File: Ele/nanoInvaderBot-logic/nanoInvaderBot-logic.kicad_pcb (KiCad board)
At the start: 2 copper layers, 72 x 40 mm, 16 parts, among them J1 S6B-ZR-SM4A-TF(LF)(SN), J2 S6B-ZR-SM4A-TF(LF)(SN), J3 1746142-1, J4 Conn_01x20, P1 USB_C_Plug_USB2.0, U4 BQ25170DSGR, U5 TLV61048DBVT

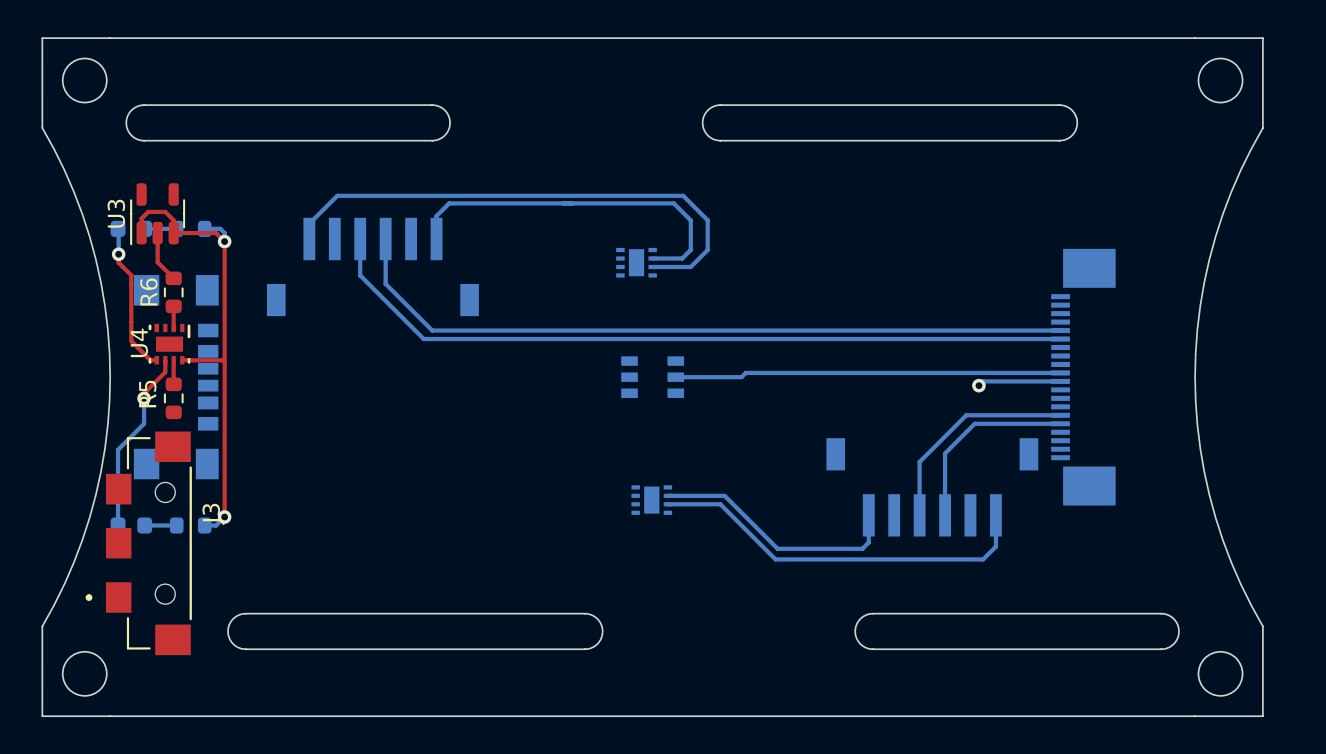
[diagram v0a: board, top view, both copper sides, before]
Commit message: Power side done, logic side cleanup
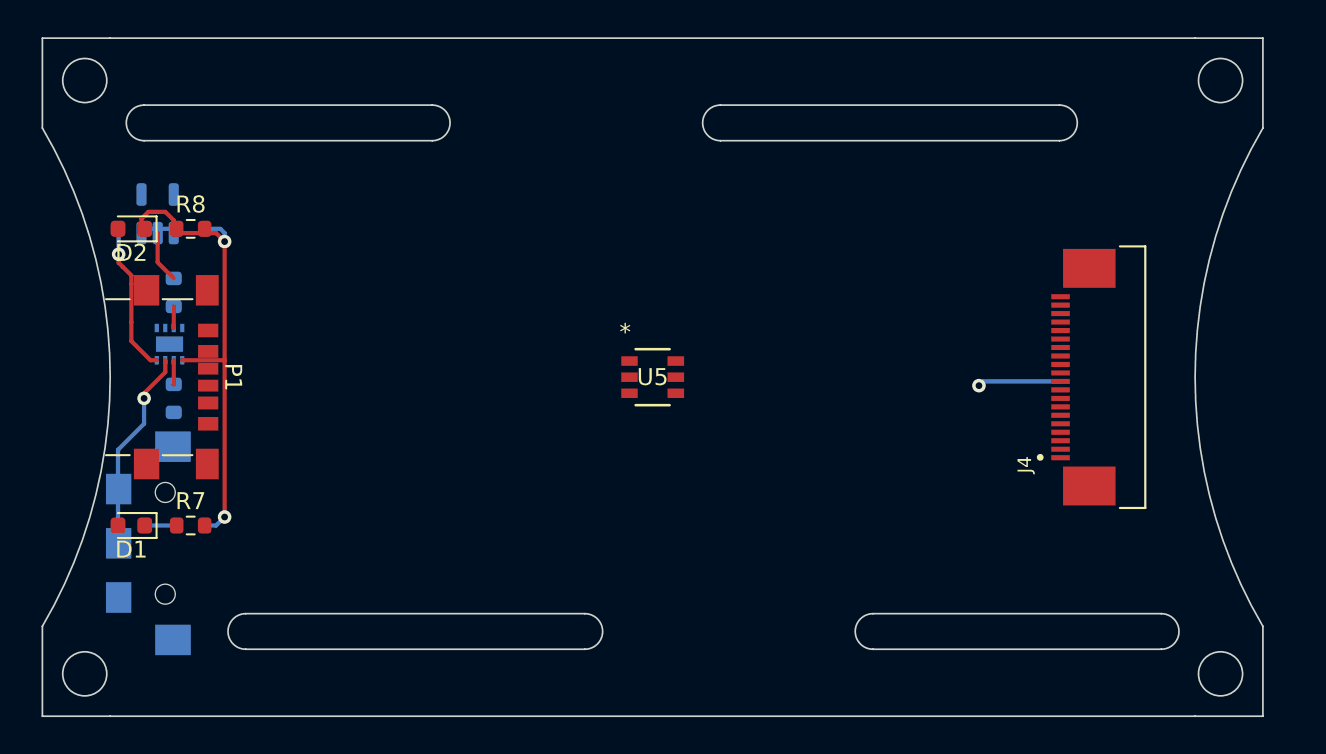
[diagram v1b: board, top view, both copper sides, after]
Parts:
- removed J1, J2: S6B-ZR-SM4A-TF(LF)(SN), footprints:JST_S6B-ZR-SM4A-TF(LF)(SN)
- removed U1, U2: ~, Package_SON:WSON-8-1EP_2x2mm_P0.5mm_EP0.9x1.6mm
- D1, D2, J4, P1, R7, R8, U5: moved to F.Cu
- J3, R5, R6, U3, U4: moved to B.Cu
- turned D1 to 180 degrees
- turned D2 to 180 degrees
- turned J3 to 90 degrees
- turned J4 to 90 degrees
- turned P1 to -90 degrees
- turned R7 to 0 degrees
- turned R8 to 0 degrees
- turned U5 to 0 degrees
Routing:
- net /MOTOR1_ENC2: track 45.0 -> 0.00 mm
- net /MOTOR1_ENC1: track 43.6 -> 0.00 mm
- net /MOTOR1_B: track 31.1 -> 0.00 mm
- net /GND: track 25.9 -> 0.00 mm
- net /MOTOR2_B: track 22.9 -> 0.00 mm
- net /MOTOR1_A: track 21.8 -> 0.00 mm
- net /MOTOR2_A: track 14.9 -> 0.00 mm
- net /MOTOR2_ENC1: track 12.6 -> 0.00 mm
- net /MOTOR2_ENC2: track 11.2 -> 0.00 mm
- net unconnected-(J3-Pad1): track 0.00 -> 10.9 mm, vias 0 -> 1
- net Net-(D1-K): track 10.9 -> 0.00 mm, vias 1 -> 0
- net /VSYS: track 0.00 -> 4.92 mm, vias 0 -> 1
- net /3V3: track 4.92 -> 0.00 mm, vias 1 -> 0
- net unconnected-(P1-SHIELD-PadS1): track 0.00 -> 4.34 mm
- net Net-(U4-ISET): track 1.27 -> 0.00 mm

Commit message: Intermediate state after v23.10
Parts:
- removed D1, D2: LED, LED_SMD:LED_0603_1608Metric
- removed J3: 1746142-1, footprints:TE_1746142-1
- removed P1: USB_C_Plug_USB2.0, Connector_USB:USB_C_Receptacle_GCT_USB4135-GF-A_6P_TopMnt_Horizontal
- removed U4: BQ25170DSGR, footprints:BQ25170DSGR_NV
- added C1: C, Capacitor_SMD:C_0805_2012Metric, F.Cu at (146.8, 101.2)
- added C2: C, Capacitor_SMD:C_0805_2012Metric, F.Cu at (151.8, 101.2)
- added C3: C, Capacitor_SMD:C_0603_1608Metric, B.Cu at (153.3, 105.2)
- added C4: 100n, Capacitor_SMD:C_0603_1608Metric, B.Cu at (138.8, 102.5)
- added C5: 100n, Capacitor_SMD:C_0603_1608Metric, B.Cu at (142.2, 96.8)
- added C6: C, Capacitor_SMD:C_0805_2012Metric, B.Cu at (128.0, 103.0)
- added C7: C, Capacitor_SMD:C_0805_2012Metric, B.Cu at (128.0, 105.0)
- added C8: C, Capacitor_SMD:C_0805_2012Metric, B.Cu at (171.8, 108.7)
- added J1: USB4110-GF-A, footprints:USB4110-GF-A_GCT, F.Cu at (122.0, 99.8)
- added L1: DFE252012P-1R0M=P2, Inductor_SMD:L_2512_6332Metric, F.Cu at (151.2, 97.5)
- added Q1: BC817W, Package_TO_SOT_SMD:SOT-323_SC-70, B.Cu at (154.5, 94.0)
- added Q2: BC817W, Package_TO_SOT_SMD:SOT-323_SC-70, B.Cu at (149.5, 94.0)
- added R1: R, Resistor_SMD:R_0402_1005Metric, B.Cu at (134.0, 91.8)
- added R10: R, Resistor_SMD:R_0402_1005Metric, F.Cu at (150.0, 103.8)
- added R11: R, Resistor_SMD:R_0402_1005Metric, B.Cu at (134.0, 93.0)
- added R12: R, Resistor_SMD:R_0402_1005Metric, B.Cu at (156.5, 106.2)
- added R13: R, Resistor_SMD:R_0402_1005Metric, B.Cu at (157.5, 106.2)
- added R2: 24k, Resistor_SMD:R_0402_1005Metric, B.Cu at (131.5, 91.8)
- added R3: 47k, Resistor_SMD:R_0402_1005Metric, B.Cu at (131.5, 93.0)
- added R4: R, Resistor_SMD:R_0402_1005Metric, B.Cu at (152.0, 92.8)
- added R9: R, Resistor_SMD:R_0402_1005Metric, F.Cu at (151.8, 103.5)
- added U1: CP2102N-Axx-xQFN28, Package_DFN_QFN:QFN-28-1EP_5x5mm_P0.5mm_EP3.35x3.35mm, B.Cu at (133.5, 100.0)
- added U2: ESP32-C3-MINI-1-N4, footprints:XCVR_ESP32-C3-MINI-1-N4, B.Cu at (171.9, 100.0)
- R5, R6: footprint Resistor_SMD:R_0603_1608Metric -> Resistor_SMD:R_0402_1005Metric
- R7, R8: footprint Resistor_SMD:R_0603_1608Metric -> Resistor_SMD:R_0402_1005Metric; moved to B.Cu
- U3: value ~ -> LSM6DS3; footprint Package_TO_SOT_SMD:SOT-23-5 -> Package_LGA:LGA-14_3x2.5mm_P0.5mm_LayoutBorder3x4y
- U5: value TLV61048DBVT -> TPS631000DRLR; footprint footprints:SOT23-6_DBV_TEX -> footprints:SOTFL50P160X60-8N
- moved R5 34.1 mm to (155.5, 106.2), turned to 90 degrees
- moved R8 29.5 mm to (152.0, 95.0), turned to 180 degrees
- moved U3 23.3 mm to (142.0, 100.0)
- moved J4 10.8 mm to (163.3, 100.0)
- moved R7 10.3 mm to (122.2, 98.5)
- moved R6 6.52 mm to (122.2, 101.5), turned to 0 degrees
- moved U5 1.46 mm to (149.2, 101.2), turned to -90 degrees
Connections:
- J4 pad 10: /GND -> /3V3
- J4 pad 12: /MOTOR2_EN_MCU -> /MOTOR2_ENC1
- J4 pad 13: /MOTOR2_B_MCU -> /MOTOR2_ENC2
- J4 pad 14: /MOTOR2_A_MCU -> /MOTOR2_B_MCU
- J4 pad 15: /MOTOR2_ENC1 -> /MOTOR2_A_MCU
- J4 pad 16: /MOTOR2_ENC2 -> /MOTOR2_EN_MCU
- J4 pad 5: /MOTOR1_ENC1 -> /MOTOR1_B_MCU
- J4 pad 6: /MOTOR1_ENC2 -> /MOTOR1_A_MCU
- J4 pad 7: /MOTOR1_A_MCU -> /MOTOR1_EN_MCU
- J4 pad 8: /MOTOR1_B_MCU -> /MOTOR1_ENC1
- J4 pad 9: /MOTOR1_EN_MCU -> /MOTOR1_ENC2
- R5 pad 1: Net-(U4-VSET) -> /3V3
- R5 pad 2: /GND -> /CHIP_PU
- R7 pad 1: /VBATT -> Net-(J1-CC1)
- R7 pad 2: Net-(D1-A) -> /GND
- R8 pad 1: /VBATT -> /RTS
- U3 pad 1: /VBATT -> /GND
- U3 pad 3: /VBATT -> /GND
- U3 pad 5: /VSYS -> /3V3
- U5 pad 1: Net-(D3-A) -> /3V3
- U5 pad 2: /GND -> Net-(U5-LX2)
- U5 pad 6: unconnected-(U5-FREQ-Pad6) -> /VSYS
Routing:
- net /3V3: track 0.00 -> 115.0 mm, vias 0 -> 3
- net /VUSB: track 0.00 -> 82.0 mm, vias 0 -> 2
- net /GND: track 0.00 -> 72.8 mm, vias 0 -> 27
- net /VSYS: track 4.92 -> 51.1 mm, vias 1 -> 0
- net /USB_RX: track 0.00 -> 43.4 mm
- net /USB_TX: track 0.00 -> 42.2 mm
- net /RTS: track 0.00 -> 36.1 mm, vias 0 -> 2
- net /IMU_SDA: track 0.00 -> 33.4 mm
- net /CHIP_PU: track 0.00 -> 31.8 mm, vias 0 -> 3
- net /IMU_SCL: track 0.00 -> 30.5 mm, vias 0 -> 2
- net /VBATT: track 29.0 -> 0.00 mm, vias 2 -> 0
- net /DTR: track 0.00 -> 23.5 mm
- net /GPIO9: track 0.00 -> 22.8 mm, vias 0 -> 4
- net /MOTOR2_ENC1: track 0.00 -> 22.7 mm, vias 0 -> 1
- net /MOTOR1_ENC1: track 0.00 -> 22.3 mm, vias 0 -> 1
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- added copper zone on B.Cu, net /GND
- added copper zone on F.Cu, net /GND
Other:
- board text added: "nanoInvaderBot v23.10 (c) Semih Iseri"
